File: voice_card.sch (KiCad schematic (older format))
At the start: 209 parts, among them J1 PCI_11_49, Q1 MMBF4391LT1G, Q10 DMMT3906, Q11 BC857BS, Q2 2N3904, Q3 BCM847, Q4 DMMT3904, Q5 DMMT3906, Q6 MMBF4391LT1G, Q7 BCM847, Q8 2N3904, Q9 DMMT3904, U1 TL074-, U10 TL072-, U11 TL074-, U12 NE555, U13 LM311M, U14 CD4052, U15 TL072-, U16 TL072-, U17 LM13700, U18 LM13700, U19 LM13700, U2 TL074-, U20 TL072-, U3 NE555, U4 LF351, U5 TL072-, U6 LM311M, U7 CD4052, U8 TL074-, U9 LF351

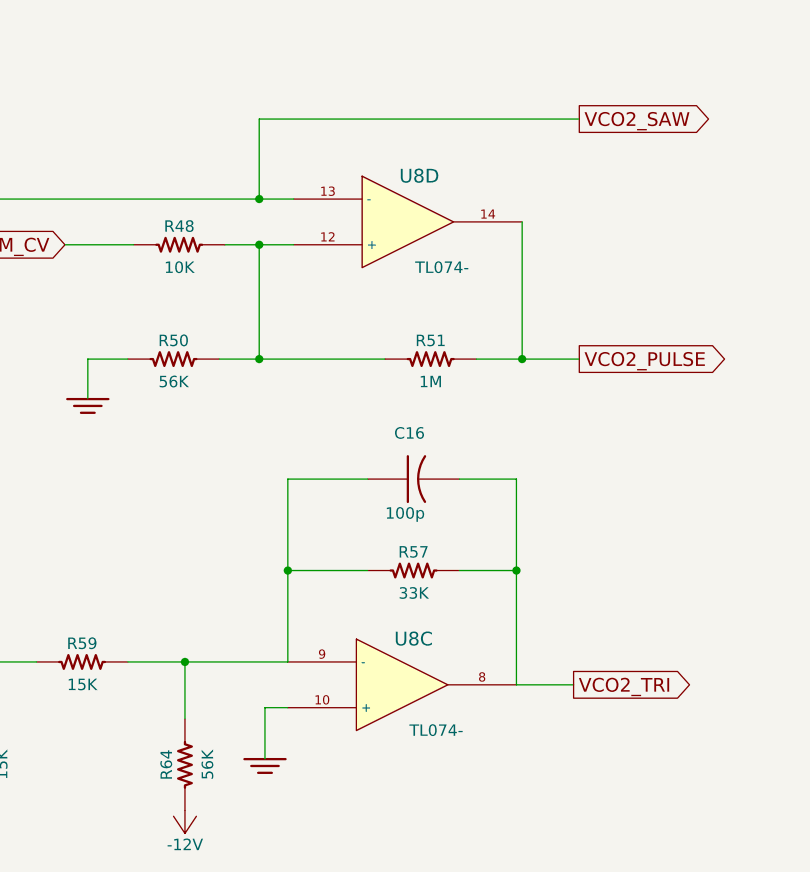
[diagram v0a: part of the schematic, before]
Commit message: VCO1 and VCO2 rough layout done. Starting to place VCF and VCA components
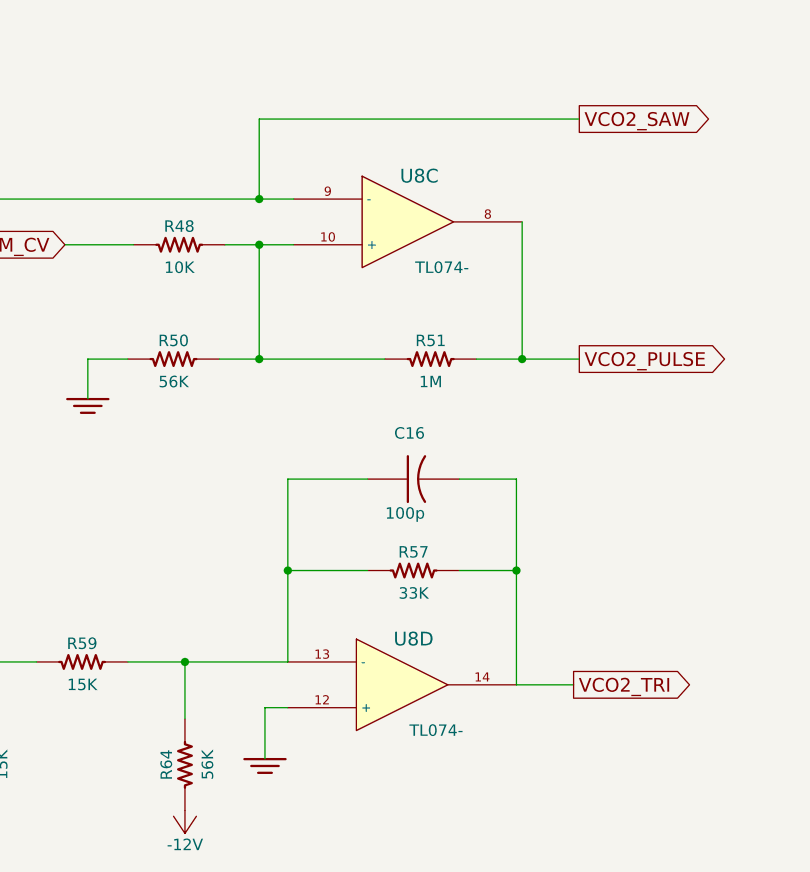
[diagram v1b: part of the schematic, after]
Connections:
- net GND: now also U8.12 (+); no longer U8.10 (+)
- net VCO2_PULSE: now also U8.8; no longer U8.14
- net VCO2_SAW: now also U8.9 (-); no longer U8.13 (-)
- net VCO2_TRI: now also U8.14; no longer U8.8
- net at C16.1, R57.1, R59.2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: now also U8.13 (-); no longer U8.9 (-)
- net at R48.1, R50.1, R51.2: now also U8.10 (+); no longer U8.12 (+)
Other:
- moved on the sheet: U8C, U8D
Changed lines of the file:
@@
 L TL074- U8
 U 4 1 564F1D31
+P 19625 11225
+F 0 "U8" H 19675 11425 60  0000 C CNN
+F 1 "TL074-" H 19775 11025 50  0000 C CNN
+F 2 "Housings_SSOP:TSSOP-14_4.4x5mm_Pitch0.65mm" H 19625 11225 60  0001 C CNN
+F 3 "" H 19625 11225 60  0000 C CNN
+	4    19625 11225
+	1    0    0    -1
+$EndComp
+$Comp
+L TL074- U8
+U 3 1 564F1D37
 P 19650 9200
 F 0 "U8" H 19700 9400 60  0000 C CNN
@@
 F 2 "Housings_SSOP:TSSOP-14_4.4x5mm_Pitch0.65mm" H 19650 9200 60  0001 C CNN
 F 3 "" H 19650 9200 60  0000 C CNN
-	4    19650 9200
+	3    19650 9200
 	1    0    0    -1
 $EndComp
-$Comp
-L TL074- U8
-U 3 1 564F1D37
-P 19625 11225
-F 0 "U8" H 19675 11425 60  0000 C CNN
-F 1 "TL074-" H 19775 11025 50  0000 C CNN
-F 2 "Housings_SSOP:TSSOP-14_4.4x5mm_Pitch0.65mm" H 19625 11225 60  0001 C CNN
-F 3 "" H 19625 11225 60  0000 C CNN
-	3    19625 11225
-	1    0    0    -1
-$EndComp

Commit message: routing vcf almost done, then need to do VCA and expo converter
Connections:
- net VCF_OUT: now also U16.1, U16.2 (-); no longer U16.6 (-), U16.7
- net at C29.1, U17.5: now also U15.5 (+); no longer U15.3 (+)
- net at R106.2, R115.1: now also U15.6 (-), U15.7; no longer U15.1, U15.2 (-)
- net at C30.1, U17.12: now also U15.3 (+); no longer U15.5 (+)
- net at R107.2, R116.1: now also U15.1, U15.2 (-); no longer U15.6 (-), U15.7
- net at C32.1, U18.12: now also U16.3 (+); no longer U16.5 (+)
- net at C31.1, U18.5: now also U16.5 (+); no longer U16.3 (+)
- net at R108.2, R117.1: now also U16.6 (-), U16.7; no longer U16.1, U16.2 (-)
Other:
- moved on the sheet: U15A, U15B, U16A, U16B
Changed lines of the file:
@@
 Connection ~ 12050 26750
 Wire Wire Line
-	14750 26400 14750 25600
+	14750 26400 14750 25900
 Wire Wire Line
-	14750 25600 15750 25600
+	14750 25900 15750 25900
 Wire Wire Line
-	15750 25600 15750 27950
+	15750 25900 15750 27950
 Wire Wire Line
 	14400 26600 14750 26600
@@
 	20300 27400 20300 27550
 Wire Wire Line
-	22250 26400 22250 25675
+	26000 26400 26000 25675
 Wire Wire Line
-	22250 25675 23250 25675
+	26000 25675 27000 25675
 Wire Wire Line
-	23250 25675 23250 27950
-Wire Wire Line
-	21900 26600 22250 26600
+	25650 26600 26000 26600
 Wire Wire Line
 	22050 27400 22050 27550
@@
 Wire Wire Line
 	23250 27950 22350 27950
-Connection ~ 23250 26500
+Connection ~ 27000 26500
 Wire Wire Line
 	21750 26550 21750 26150
@@
 	21750 25350 21750 25750
 Wire Wire Line
-	23500 26750 23250 26750
-Connection ~ 23250 26750
+	27250 26750 27000 26750
+Connection ~ 27000 26750
 Wire Wire Line
 	24550 26450 24300 26450
@@
 	24050 27400 24050 27550
 Wire Wire Line
-	26000 26400 26000 26100
+	22250 26400 22250 26100
 Wire Wire Line
-	26000 26100 27000 26100
+	22250 26100 23250 26100
 Wire Wire Line
-	27000 26100 27000 27950
+	23250 26100 23250 27950
 Wire Wire Line
-	25650 26600 26000 26600
+	21900 26600 22250 26600
 Wire Wire Line
 	25800 27400 25800 27550
@@
 Wire Wire Line
 	26100 27950 27200 27950
-Connection ~ 27000 26500
+Connection ~ 23250 26500
 Wire Wire Line
 	25500 26550 25500 26150
@@
 	25500 25350 25500 25750
 Wire Wire Line
-	27250 26750 27000 26750
-Connection ~ 27000 26750
+	23500 26750 23250 26750
+Connection ~ 23250 26750
 Connection ~ 27000 27950
 Wire Wire Line
@@
 Connection ~ 25500 25350
 Wire Wire Line
-	18500 26400 18500 26100
+	18500 26400 18500 25625
 Wire Wire Line
-	18500 26100 19500 26100
+	18500 25625 19500 25625
 Wire Wire Line
-	19500 26100 19500 27950
+	19500 25625 19500 27950
 Wire Wire Line
 	27650 26750 28350 26750
@@
 L TL072- U15
 U 1 1 56506B9E
-P 15250 26500
-F 0 "U15" H 15200 26700 60  0000 L CNN
-F 1 "TL072-" H 15200 26250 60  0000 L CNN
-F 2 "MyModules:TSSOP8-JRL" H 15250 26500 60  0001 C CNN
-F 3 "" H 15250 26500 60  0000 C CNN
-	1    15250 26500
-	1    0    0    -1
-$EndComp
-$Comp
-L TL072- U15
-U 2 1 56506B9F
 P 19000 26500
 F 0 "U15" H 18950 26700 60  0000 L CNN
@@
 F 2 "MyModules:TSSOP8-JRL" H 19000 26500 60  0001 C CNN
 F 3 "" H 19000 26500 60  0000 C CNN
-	2    19000 26500
+	1    19000 26500
 	1    0    0    -1
 $EndComp
 $Comp
-L TL072- U16
-U 1 1 56506BA0
-P 22750 26500
-F 0 "U16" H 22700 26700 60  0000 L CNN
-F 1 "TL072-" H 22700 26250 60  0000 L CNN
-F 2 "MyModules:TSSOP8-JRL" H 22750 26500 60  0001 C CNN
-F 3 "" H 22750 26500 60  0000 C CNN
-	1    22750 26500
+L TL072- U15
+U 2 1 56506B9F
+P 15250 26500
+F 0 "U15" H 15200 26700 60  0000 L CNN
+F 1 "TL072-" H 15200 26250 60  0000 L CNN
+F 2 "MyModules:TSSOP8-JRL" H 15250 26500 60  0001 C CNN
+F 3 "" H 15250 26500 60  0000 C CNN
+	2    15250 26500
 	1    0    0    -1
 $EndComp
 $Comp
 L TL072- U16
-U 2 1 56506BA4
+U 1 1 56506BA0
 P 26500 26500
 F 0 "U16" H 26450 26700 60  0000 L CNN
@@
 F 2 "MyModules:TSSOP8-JRL" H 26500 26500 60  0001 C CNN
 F 3 "" H 26500 26500 60  0000 C CNN
-	2    26500 26500
+	1    26500 26500
+	1    0    0    -1
+$EndComp
+$Comp
+L TL072- U16
+U 2 1 56506BA4
+P 22750 26500
+F 0 "U16" H 22700 26700 60  0000 L CNN
+F 1 "TL072-" H 22700 26250 60  0000 L CNN
+F 2 "MyModules:TSSOP8-JRL" H 22750 26500 60  0001 C CNN
+F 3 "" H 22750 26500 60  0000 C CNN
+	2    22750 26500
 	1    0    0    -1
 $EndComp
@@
 L +12V #PWR083
 U 1 1 56516DE4
-P 15150 26100
-F 0 "#PWR083" H 15150 25950 50  0001 C CNN
-F 1 "+12V" H 15150 26240 50  0000 C CNN
-F 2 "" H 15150 26100 60  0000 C CNN
-F 3 "" H 15150 26100 60  0000 C CNN
-	1    15150 26100
+P 18900 26100
+F 0 "#PWR083" H 18900 25950 50  0001 C CNN
+F 1 "+12V" H 18900 26240 50  0000 C CNN
+F 2 "" H 18900 26100 60  0000 C CNN
+F 3 "" H 18900 26100 60  0000 C CNN
+	1    18900 26100
 	1    0    0    -1
 $EndComp
@@
 L +12V #PWR085
 U 1 1 5651855A
-P 22650 26100
-F 0 "#PWR085" H 22650 25950 50  0001 C CNN
-F 1 "+12V" H 22650 26240 50  0000 C CNN
-F 2 "" H 22650 26100 60  0000 C CNN
-F 3 "" H 22650 26100 60  0000 C CNN
-	1    22650 26100
+P 26400 26100
+F 0 "#PWR085" H 26400 25950 50  0001 C CNN
+F 1 "+12V" H 26400 26240 50  0000 C CNN
+F 2 "" H 26400 26100 60  0000 C CNN
+F 3 "" H 26400 26100 60  0000 C CNN
+	1    26400 26100
 	1    0    0    -1
 $EndComp
@@
 L -12V #PWR087
 U 1 1 56518E78
-P 15150 26900
-F 0 "#PWR087" H 15150 27000 30  0001 C CNN
-F 1 "-12V" H 15150 27050 50  0000 C CNN
-F 2 "~" H 15150 26900 60  0000 C CNN
-F 3 "~" H 15150 26900 60  0000 C CNN
-	1    15150 26900
+P 18900 26900
+F 0 "#PWR087" H 18900 27000 30  0001 C CNN
+F 1 "-12V" H 18900 27050 50  0000 C CNN
+F 2 "~" H 18900 26900 60  0000 C CNN
+F 3 "~" H 18900 26900 60  0000 C CNN
+	1    18900 26900
 	-1   0    0    1
 $EndComp
@@
 L -12V #PWR090
 U 1 1 5651BD89
-P 22650 26900
-F 0 "#PWR090" H 22650 27000 30  0001 C CNN
-F 1 "-12V" H 22650 27050 50  0000 C CNN
-F 2 "~" H 22650 26900 60  0000 C CNN
-F 3 "~" H 22650 26900 60  0000 C CNN
-	1    22650 26900
+P 26400 26900
+F 0 "#PWR090" H 26400 27000 30  0001 C CNN
+F 1 "-12V" H 26400 27050 50  0000 C CNN
+F 2 "~" H 26400 26900 60  0000 C CNN
+F 3 "~" H 26400 26900 60  0000 C CNN
+	1    26400 26900
 	-1   0    0    1
 $EndComp
@@
 	36100 8450 35700 8450
 Wire Wire Line
-	35700 8450 35700 8950
+	35700 8950 35700 8450
 Wire Wire Line
 	36700 8850 36800 8850
@@
 	30800 9450 36100 9450
 Wire Wire Line
-	35700 8950 35250 8950
+	35250 8950 35700 8950
 Wire Wire Line
 	35550 7750 35550 8300
@@
 	32450 5650 32600 5650
 Wire Wire Line
-	32600 5650 32600 4450
+	32600 4450 32600 5650
 Wire Wire Line
-	32600 4450 29700 4450
+	29700 4450 32600 4450
 Wire Wire Line
 	29700 4450 29700 4500
@@
 	35700 16250 35300 16250
 Wire Wire Line
-	35300 16250 35300 16750
+	35300 16750 35300 16250
 Wire Wire Line
 	36300 16650 36400 16650
@@
 	30400 17250 35700 17250
 Wire Wire Line
-	35300 16750 34850 16750
+	34850 16750 35300 16750
 Wire Wire Line
 	35150 15550 35150 16100
@@
 	32050 13450 32200 13450
 Wire Wire Line
-	32200 13450 32200 12250
+	32200 12250 32200 13450
 Wire Wire Line
-	32200 12250 29300 12250
+	29300 12250 32200 12250
 Wire Wire Line
 	29300 12250 29300 12300
@@
 Connection ~ 10275 25450
 Connection ~ 34400 16750
+Wire Wire Line
+	27000 25675 27000 27950
 $EndSCHEMATC

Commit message: finishing up VCF/VCA layout and routing
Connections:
- net GND: now also U20.5 (+); no longer U20.3 (+)
- net VCA_OUT: now also U20.1, U20.2 (-); no longer U20.6 (-), U20.7
- net at C33.1, R122.1, U19.12: now also U20.3 (+); no longer U20.5 (+)
- net at C34.2, Q11.6 (C1), R125.1: now also U20.6 (-); no longer U20.2 (-)
- net at C34.1, R121.2: now also U20.7; no longer U20.1
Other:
- moved on the sheet: U20A, U20B

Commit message: struggling with EG component layout and routing. Thinking of replacing U2 (TL074) with two TL072s for ease of compact layout
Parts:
- removed R32, R83: 1K, MyModules:SM0603-R-JRL, symbol R_US
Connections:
- net EG1_ENV_OUT: now also C8.1, R44.2, R5.1, U2.7, U3.6 (THR)
- net EG1_INV_OUT: now also U2.14; no longer U2.1
- net EG2_ENV_OUT: now also C27.1, R68.1, R92.2, U11.7, U12.6 (THR)
- net GND: now also Q5.1, U2.3 (+); no longer Q5.2, U2.10 (+)
- net at R1.1, R5.2: now also U2.13 (-); no longer U2.2 (-)
- net at R14.2, R7.2: now also U2.12 (+); no longer U2.3 (+)
- net at C14.1, R37.1: now also U2.1; no longer U2.8
- net at C14.2, Q4.6, R45.1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: now also Q5.6, U2.2 (-); no longer Q5.3, U2.9 (-)
- net at R47.1, R49.2: now also U2.10 (+); no longer U2.12 (+)
- net at R41.2, R44.1: now also U2.9 (-); no longer U2.13 (-)
- net at R41.1, R45.2, TP7.1: now also U2.8; no longer U2.14
- net at Q4.4, Q4.5, R37.2: now also Q5.4, Q5.5; no longer Q5.4, Q5.5
- net at C8.2, Q4.3, U2.6 (-): now also Q5.3; no longer Q5.6
- net at R40.2, R42.2, R43.2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: now also Q5.2; no longer Q5.1
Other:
- moved on the sheet: R41, R45, R49, TP6, TP7, U2A, U2C, U2D

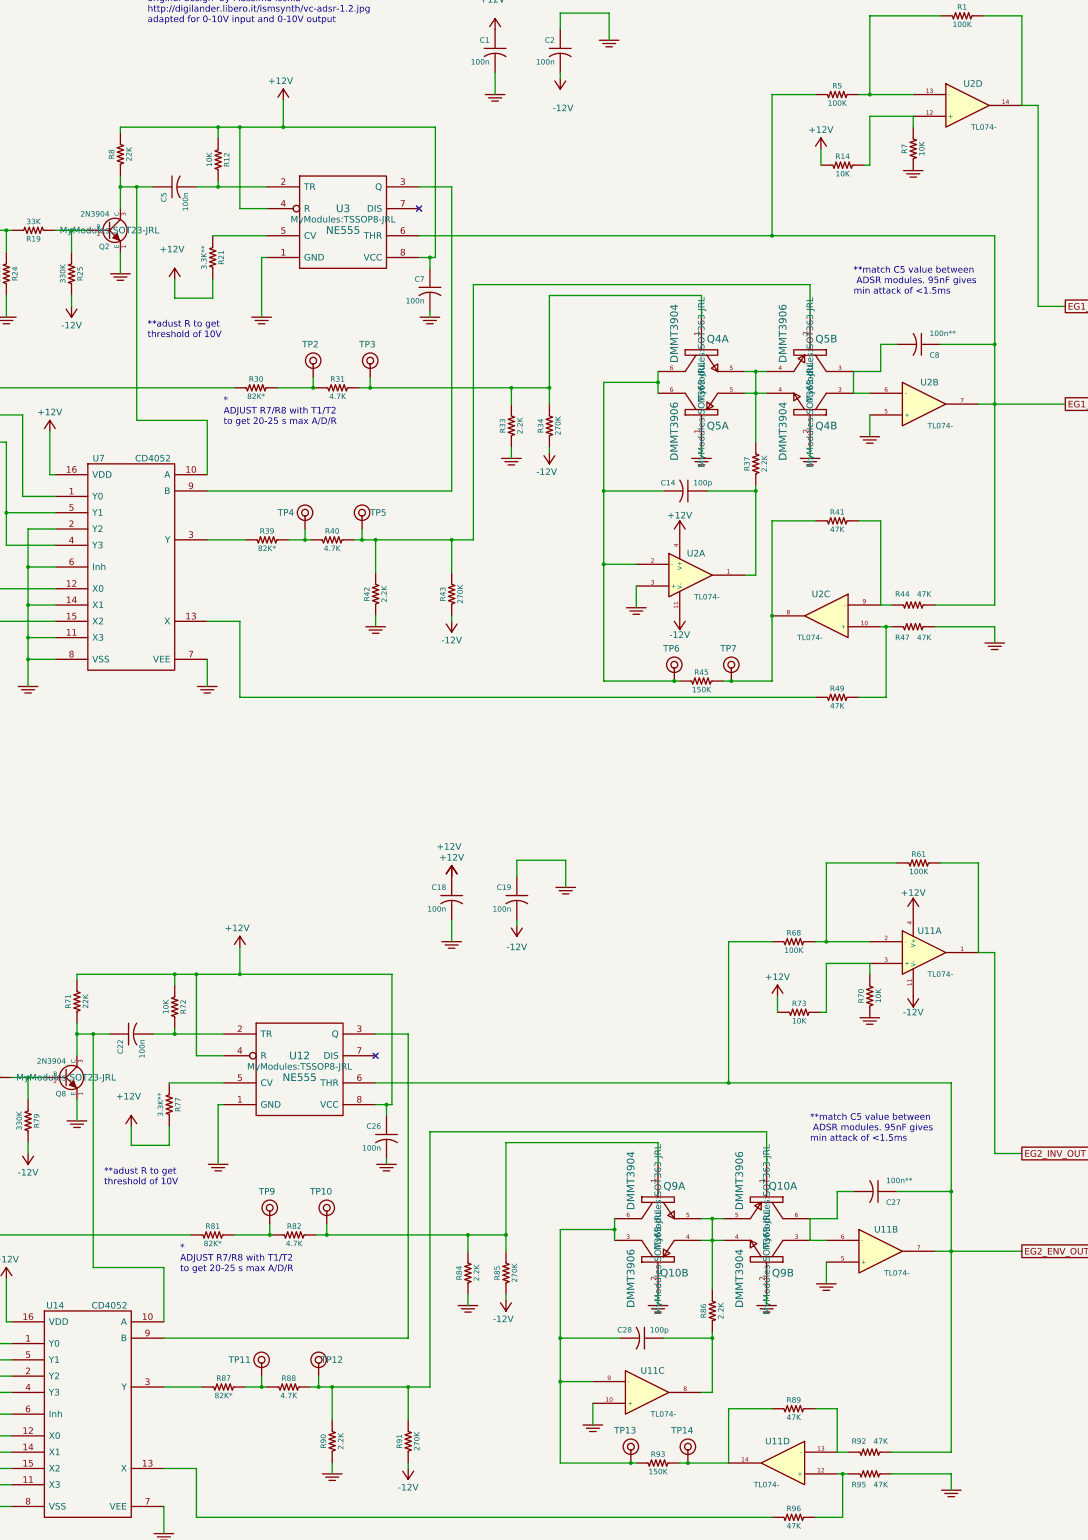
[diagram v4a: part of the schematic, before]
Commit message: EG1 routed, just flipping and fitting now
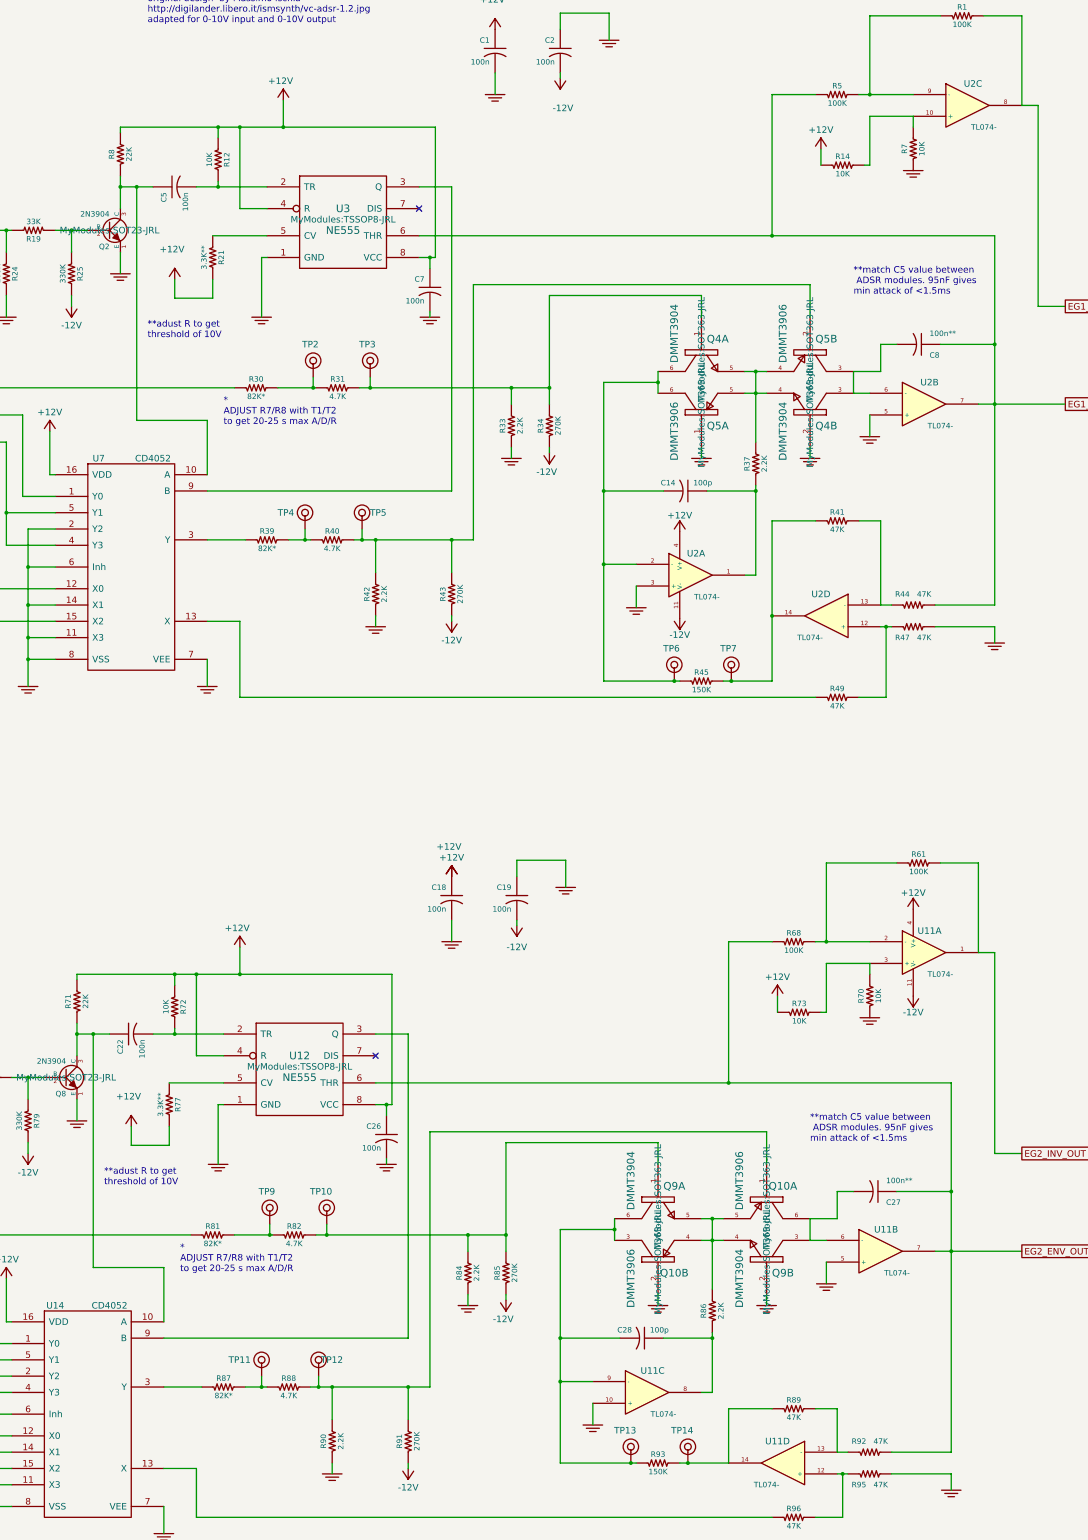
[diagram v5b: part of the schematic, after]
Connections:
- net EG1_INV_OUT: now also U2.8; no longer U2.14
- net at R14.2, R7.2: now also U2.10 (+); no longer U2.12 (+)
- net at R1.1, R5.2: now also U2.9 (-); no longer U2.13 (-)
- net at R41.1, R45.2, TP7.1: now also U2.14; no longer U2.8
- net at R41.2, R44.1: now also U2.13 (-); no longer U2.9 (-)
- net at R47.1, R49.2: now also U2.12 (+); no longer U2.10 (+)
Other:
- moved on the sheet: U2C, U2D
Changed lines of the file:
@@
 L TL074- U2
 U 4 1 56535530
-P 37500 4250
-F 0 "U2" H 37550 4450 60  0000 C CNN
-F 1 "TL074-" H 37650 4050 50  0000 C CNN
-F 2 "Housings_SSOP:TSSOP-14_4.4x5mm_Pitch0.65mm" H 37500 4250 60  0001 C CNN
-F 3 "" H 37500 4250 60  0000 C CNN
-	4    37500 4250
-	1    0    0    -1
+P 36200 8950
+F 0 "U2" H 36250 9150 60  0000 C CNN
+F 1 "TL074-" H 36350 8750 50  0000 C CNN
+F 2 "Housings_SSOP:TSSOP-14_4.4x5mm_Pitch0.65mm" H 36200 8950 60  0001 C CNN
+F 3 "" H 36200 8950 60  0000 C CNN
+	4    36200 8950
+	-1   0    0    -1
 $EndComp
 $Comp
@@
 L TL074- U2
 U 3 1 56535536
-P 36200 8950
-F 0 "U2" H 36250 9150 60  0000 C CNN
-F 1 "TL074-" H 36350 8750 50  0000 C CNN
-F 2 "Housings_SSOP:TSSOP-14_4.4x5mm_Pitch0.65mm" H 36200 8950 60  0001 C CNN
-F 3 "" H 36200 8950 60  0000 C CNN
-	3    36200 8950
-	-1   0    0    -1
+P 37500 4250
+F 0 "U2" H 37550 4450 60  0000 C CNN
+F 1 "TL074-" H 37650 4050 50  0000 C CNN
+F 2 "Housings_SSOP:TSSOP-14_4.4x5mm_Pitch0.65mm" H 37500 4250 60  0001 C CNN
+F 3 "" H 37500 4250 60  0000 C CNN
+	3    37500 4250
+	1    0    0    -1
 $EndComp
 $Comp
@@
 	36100 8075 35700 8075
 Wire Wire Line
-	35700 9550 35700 8075
+	35700 8075 35700 9550
 Wire Wire Line
 	36700 8850 36800 8850
@@
 	30800 9700 36100 9700
 Wire Wire Line
-	35250 9550 35700 9550
+	35700 9550 35250 9550
 Wire Wire Line
 	35550 7750 35550 8575
@@
 	32450 5650 32600 5650
 Wire Wire Line
-	32600 4450 32600 5650
-Wire Wire Line
-	29700 4450 32600 4450
+	32600 5650 32600 4450
+Wire Wire Line
+	32600 4450 29700 4450
 Wire Wire Line
 	29700 4450 29700 4500
@@
 	35700 16250 35300 16250
 Wire Wire Line
-	35300 16750 35300 16250
+	35300 16250 35300 16750
 Wire Wire Line
 	36300 16650 36400 16650
@@
 	30400 17250 35700 17250
 Wire Wire Line
-	34850 16750 35300 16750
+	35300 16750 34850 16750
 Wire Wire Line
 	35150 15550 35150 16100
@@
 	32050 13450 32200 13450
 Wire Wire Line
-	32200 12250 32200 13450
-Wire Wire Line
-	29300 12250 32200 12250
+	32200 13450 32200 12250
+Wire Wire Line
+	32200 12250 29300 12250
 Wire Wire Line
 	29300 12250 29300 12300

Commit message: starting to place components for EG2
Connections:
- net EG2_INV_OUT: now also U11.8; no longer U11.1
- net GND: now also U11.3 (+); no longer U11.10 (+)
- net at R61.1, R68.2: now also U11.9 (-); no longer U11.2 (-)
- net at R70.2, R73.2: now also U11.10 (+); no longer U11.3 (+)
- net at C28.1, R86.1: now also U11.1; no longer U11.8
- net at C28.2, Q10.3, Q9.6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: now also U11.2 (-); no longer U11.9 (-)
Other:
- moved on the sheet: R89, R92, R93, R95, R96, TP13, TP14, U11A, U11C, U11D
